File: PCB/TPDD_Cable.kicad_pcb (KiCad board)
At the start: 2 copper layers, 10.3 x 15 mm, 11 parts, among them J1 TPDD_RS-232C, P3 RX, P4 RTS, P5 CTS, P6 DSR, Q1 DTA114EKA, Q2 DTA114EKA, Q3 DTA114EKA

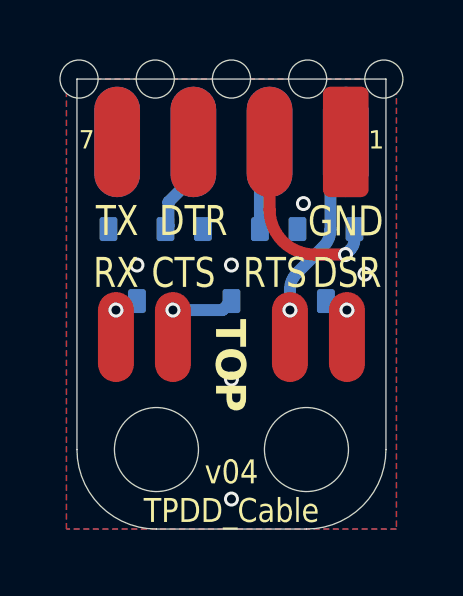
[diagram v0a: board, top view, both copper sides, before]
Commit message: transistors & wire pads placement
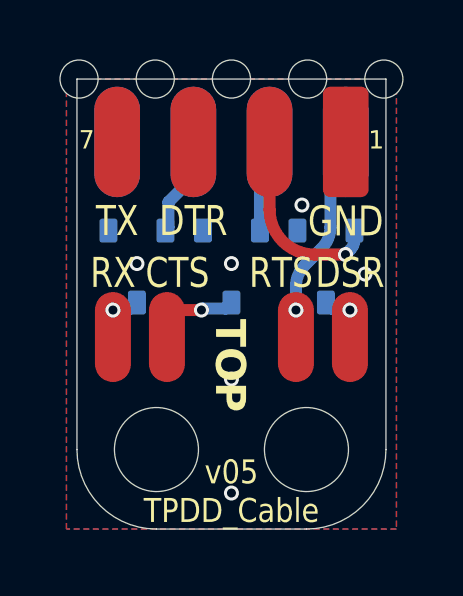
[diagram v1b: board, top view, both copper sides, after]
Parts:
- moved P5 0.20 mm to (142.8, 88.2)
- moved P4 0.20 mm to (147.1, 88.2)
- moved P6 0.10 mm to (148.9, 88.2)
- moved P3 0.10 mm to (141.0, 88.2)
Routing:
- net /CTS: track 2.07 -> 3.15 mm

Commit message: correct DTE vs DCE signal names & DE9 pinout in schematic
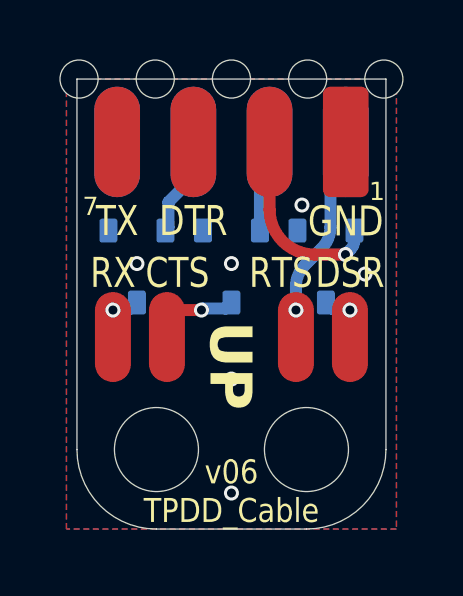
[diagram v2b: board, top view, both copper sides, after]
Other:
- board text added: "DOWN"
- board text added: "UP"
- board text removed: "BOTTOM"
- board text removed: "TOP"

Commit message: db25 pinout pics, enlarge ziptie holes to 3mm
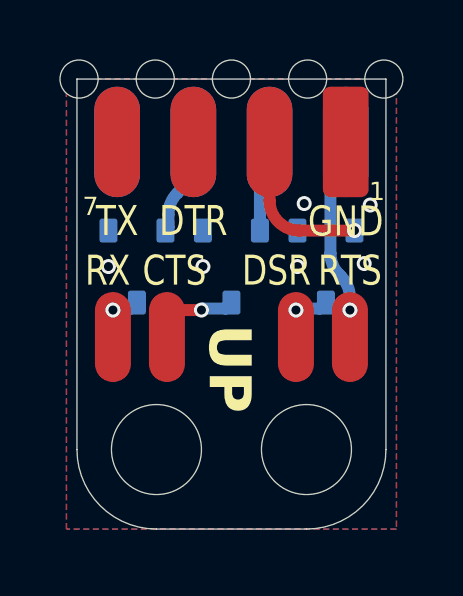
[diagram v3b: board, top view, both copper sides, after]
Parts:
- moved P4 1.80 mm to (148.9, 88.2)
- moved P6 1.80 mm to (147.1, 88.2)
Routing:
- net /DSR_TTL: track 6.48 -> 5.32 mm
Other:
- board text added: "github bkw777 TPDD_Cable v${REVISION}"
- board text removed: "github.com bkw777 TPDD_Cable"
- board text removed: "v${REVISION} TPDD_Cable"

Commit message: move via out of smt pad
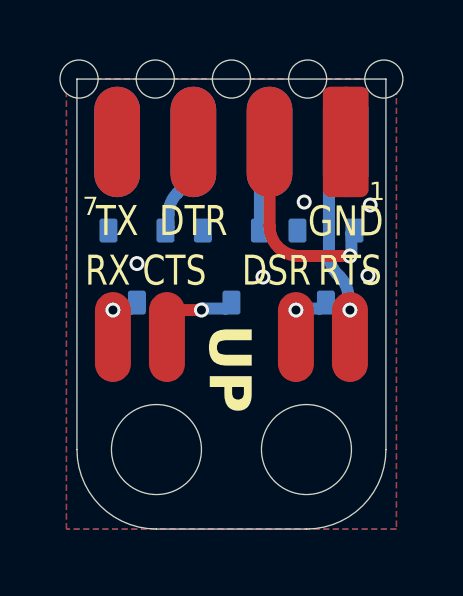
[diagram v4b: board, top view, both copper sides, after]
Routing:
- net /DSR_TTL: track 5.32 -> 6.93 mm
- net GND: vias 6 -> 5
